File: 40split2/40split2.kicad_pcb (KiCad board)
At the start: 2 copper layers, 145.3 x 97 mm, 54 parts

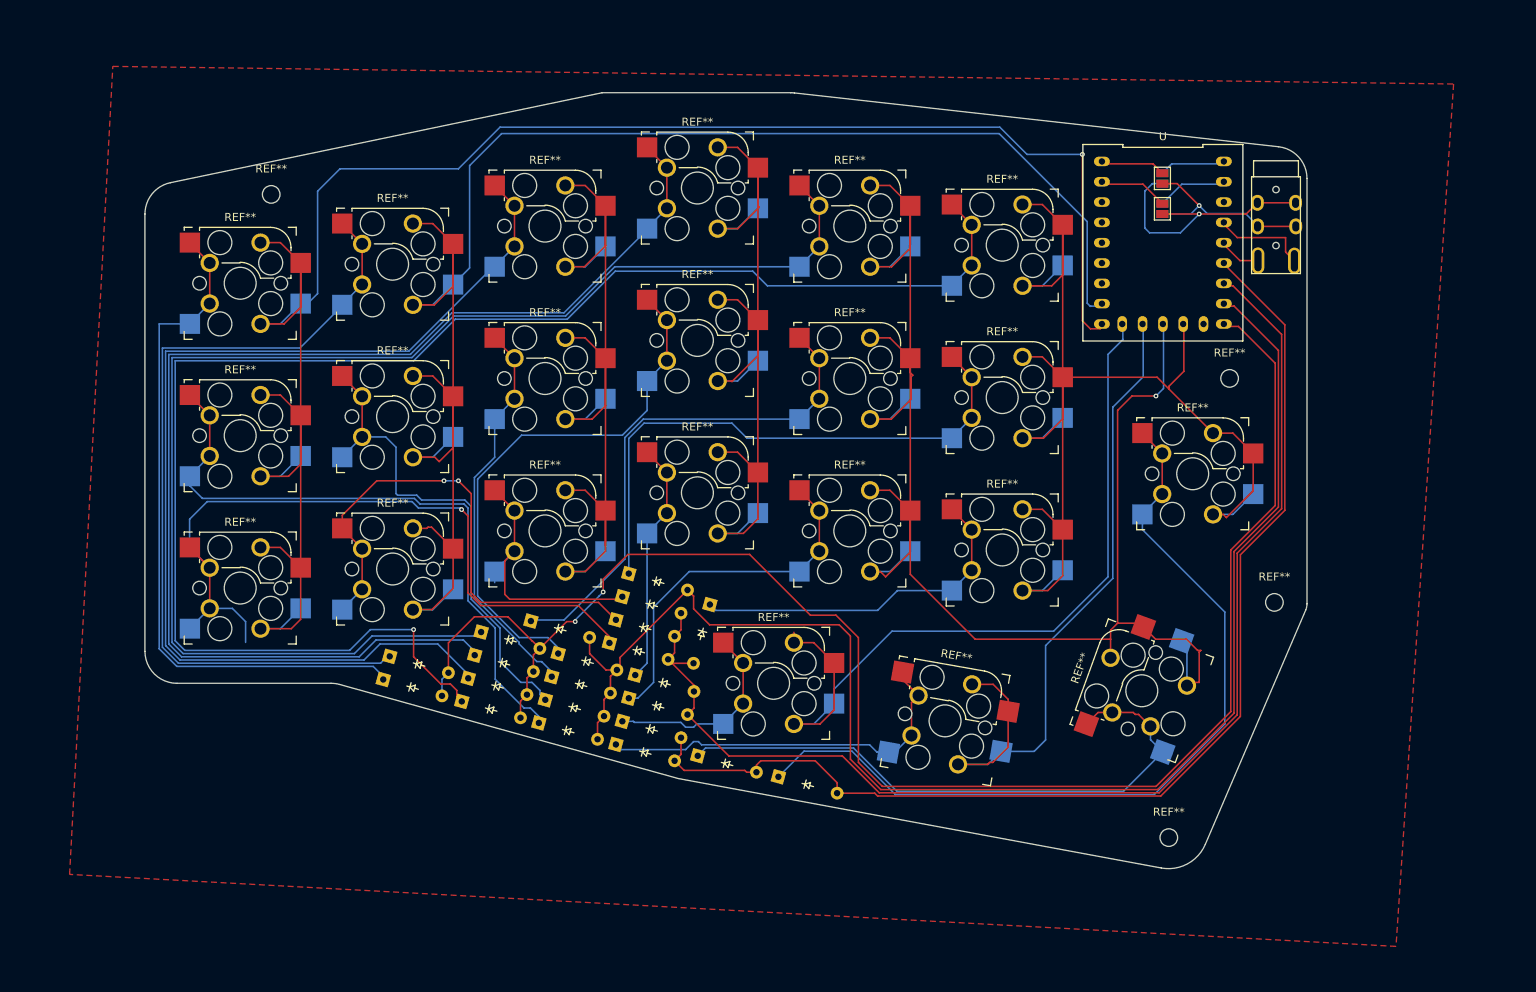
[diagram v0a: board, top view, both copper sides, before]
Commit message: Keyboard V4: Rearrange diodes
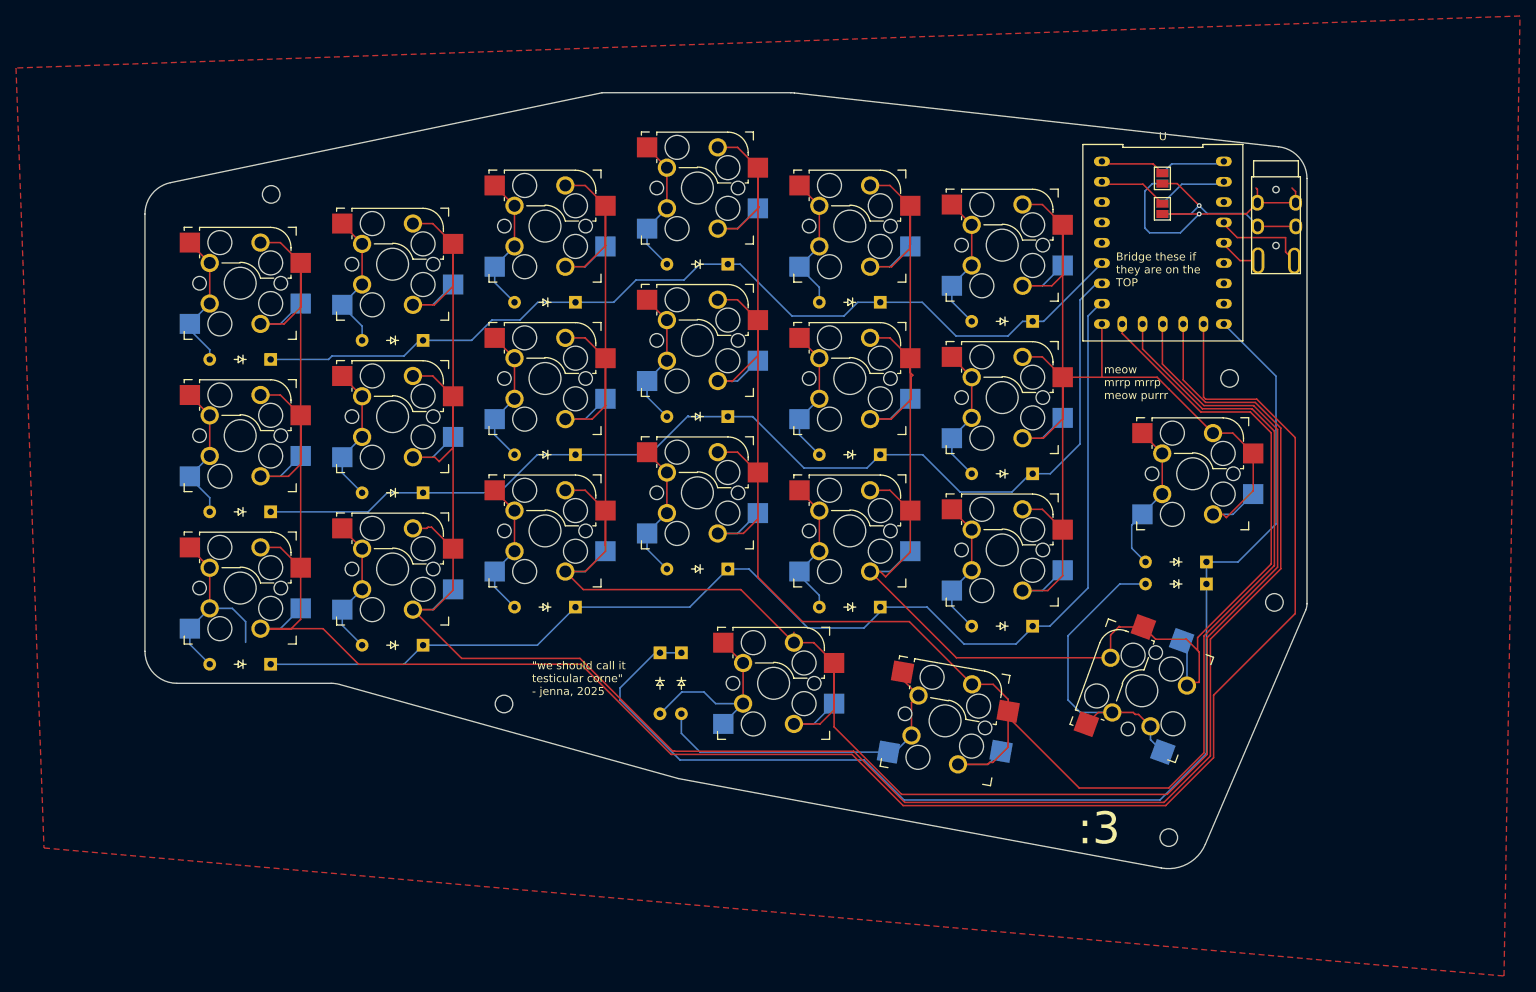
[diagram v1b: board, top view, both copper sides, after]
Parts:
- removed the REF** at (121.8, 134.7)
- removed the REF** at (114.6, 123.4)
- removed the REF** at (131.5, 137.4)
- removed the REF** at (143.2, 119.9)
- removed the REF** at (151.8, 141.5)
- removed the REF** at (112.2, 132.0)
- removed the REF** at (123.5, 129.0)
- removed the REF** at (122.7, 131.8)
- removed the REF** at (120.9, 122.0)
- removed the REF** at (133.1, 131.6)
- removed the REF** at (113.0, 129.2)
- removed the REF** at (124.3, 126.1)
- removed the REF** at (113.8, 126.3)
- removed the REF** at (133.9, 128.8)
- removed the REF** at (133.1, 116.1)
- removed the REF** at (141.7, 138.8)
- removed the REF** at (103.2, 126.4)
- removed the REF** at (131.5, 121.8)
- removed the REF** at (102.4, 129.3)
- removed the REF** at (130.7, 124.7)
- removed the REF** at (132.3, 119.0)
- removed the REF** at (132.3, 134.5)
- added REF**: 1N4148, Scotto_lib:Diode_DO-35, F.Cu at (164.5, 101.2)
- added REF**: 1N4148, Scotto_lib:Diode_DO-35, F.Cu at (126.4, 120.3)
- added REF**: 1N4148, Scotto_lib:Diode_DO-35, F.Cu at (139.7, 126.0)
- added REF**: 1N4148, Scotto_lib:Diode_DO-35, F.Cu at (164.5, 120.3)
- added REF**: 1N4148, Scotto_lib:Diode_DO-35, F.Cu at (145.5, 96.4)
- added REF**: MountingHole_2.2mm_M2, kicad_screws:MountingHole_2.2mm_M2, F.Cu at (117.5, 132.4)
- added REF**: 1N4148, Scotto_lib:Diode_DO-35, F.Cu at (107.4, 106.0)
- added REF**: 1N4148, Scotto_lib:Diode_DO-35, F.Cu at (183.6, 103.6)
- added REF**: 1N4148, Scotto_lib:Diode_DO-35, F.Cu at (107.4, 86.9)
- added REF**: 1N4148, Scotto_lib:Diode_DO-35, F.Cu at (107.4, 125.0)
- added REF**: 1N4148, Scotto_lib:Diode_DO-35, F.Cu at (164.5, 82.2)
- added REF**: 1N4148, Scotto_lib:Diode_DO-35, F.Cu at (183.6, 84.5)
- added REF**: 1N4148, Scotto_lib:Diode_DO-35, F.Cu at (205.3, 114.6)
- added REF**: 1N4148, Scotto_lib:Diode_DO-35, F.Cu at (126.4, 101.2)
- added REF**: 1N4148, Scotto_lib:Diode_DO-35, F.Cu at (205.3, 117.4)
- added REF**: 1N4148, Scotto_lib:Diode_DO-35, F.Cu at (126.4, 82.2)
- added REF**: 1N4148, Scotto_lib:Diode_DO-35, F.Cu at (88.3, 108.4)
- added REF**: 1N4148, Scotto_lib:Diode_DO-35, F.Cu at (88.3, 89.3)
- added REF**: 1N4148, Scotto_lib:Diode_DO-35, F.Cu at (88.3, 127.4)
- added REF**: 1N4148, Scotto_lib:Diode_DO-35, F.Cu at (145.5, 77.4)
- added REF**: 1N4148, Scotto_lib:Diode_DO-35, F.Cu at (145.5, 115.5)
- added REF**: 1N4148, Scotto_lib:Diode_DO-35, F.Cu at (137.0, 126.0)
- added REF**: 1N4148, Scotto_lib:Diode_DO-35, F.Cu at (183.6, 122.6)
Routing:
- net (no net): track 3853.1 -> 2673.8 mm, vias 10 -> 2
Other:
- board text added: ":3"
- board text added: ":3 :3 :3"
- board text added: "Bridge these if they are on the TOP"
- board text added: "github.com/junnnaaaaaa github.com/HamNuggets"
- board text added: "meow mrrp mrrp meow purrr"
- board text added: "{dblquote}We are NOT calling it testicular corne{dblquote} - jade, 2025"
- board text added: "{dblquote}we should call it testicular corne{dblquote} - jenna, 2025"

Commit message: qmk begins.. a battle awaits
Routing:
- net (no net): track 2673.8 -> 2673.2 mm
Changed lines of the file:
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@@
-	)
-	(segment
-		(start 209.14625 74.07)
-		(end 207.55 72.47375)
-		(width 0.2)
-		(layer "F.Cu")
-		(net 0)
 	)
 	(segment
@@
 	)
 	(segment
+		(start 211.665 67.695)
+		(end 211.99 67.37)
+		(width 0.2)
+		(layer "F.Cu")
+		(net 0)
+	)
+	(segment
 		(start 92.075 96.28625)
 		(end 92.075 102.385)
@@
 	)
 	(segment
+		(start 213.15 74.71)
+		(end 213.49 74.37)
+		(width 0.2)
+		(layer "F.Cu")
+		(net 0)
+	)
+	(segment
 		(start 106.105 120.575)
 		(end 112.2 126.67)
@@
 	)
 	(segment
-		(start 215.19 75.87)
-		(end 215.19 74.07)
-		(width 0.2)
-		(layer "F.Cu")
-		(net 0)
-	)
-	(segment
 		(start 158.75 127.2425)
 		(end 158.75 135.23)
@@
 	)
 	(segment
-		(start 216.44 68.32)
-		(end 215.99 67.87)
-		(width 0.2)
-		(layer "F.Cu")
-		(net 0)
-	)
-	(segment
 		(start 154.425 86.6025)
 		(end 154.425 86.6625)
@@
 	)
 	(segment
+		(start 214.49 74.37)
+		(end 216.29 76.17)
+		(width 0.2)
+		(layer "F.Cu")
+		(net 0)
+	)
+	(segment
 		(start 175.955 72.47375)
 		(end 175.955 77.55375)
@@
 	)
 	(segment
+		(start 216.44 67.82)
+		(end 215.99 67.37)
+		(width 0.2)
+		(layer "F.Cu")
+		(net 0)
+	)
+	(segment
 		(start 87.055 84.85625)
 		(end 90.00375 84.85625)
@@
 	)
 	(segment
-		(start 211.665 68.045)
-		(end 211.49 67.87)
-		(width 0.2)
-		(layer "F.Cu")
-		(net 0)
-	)
-	(segment
 		(start 168.19 75.07)
 		(end 168.275 74.985)
@@
 	)
 	(segment
-		(start 216.44 69.72)
-		(end 216.44 68.32)
-		(width 0.2)
-		(layer "F.Cu")
-		(net 0)
-	)
-	(segment
 		(start 192.31 67.39375)
 		(end 197.36375 67.39375)
@@
 	)
 	(segment
+		(start 216.29 76.17)
+		(end 216.29 76.97)
+		(width 0.2)
+		(layer "F.Cu")
+		(net 0)
+	)
+	(segment
 		(start 192.19 91.52375)
 		(end 199.1325 91.52375)
@@
 	)
 	(segment
-		(start 215.19 74.07)
-		(end 209.14625 74.07)
-		(width 0.2)
-		(layer "F.Cu")
-		(net 0)
-	)
-	(segment
 		(start 173.475 69.93375)
 		(end 173.475 69.99375)
@@
 	)
 	(segment
-		(start 211.665 69.72)
-		(end 211.665 68.045)
-		(width 0.2)
-		(layer "F.Cu")
-		(net 0)
-	)
-	(segment
 		(start 180.507463 133.987463)
 		(end 180.507463 133.285665)
@@
 	)
 	(segment
+		(start 207.47 77.25)
+		(end 211.435 77.25)
+		(width 0.2)
+		(layer "F.Cu")
+		(net 0)
+	)
+	(segment
 		(start 190.291445 134.888403)
 		(end 191.753151 133.426697)
@@
 	)
 	(segment
+		(start 213.49 74.37)
+		(end 214.49 74.37)
+		(width 0.2)
+		(layer "F.Cu")
+		(net 0)
+	)
+	(segment
 		(start 153.73 124.7025)
 		(end 156.21 124.7025)
@@
 	)
 	(segment
+		(start 216.44 69.72)
+		(end 216.44 67.82)
+		(width 0.2)
+		(layer "F.Cu")
+		(net 0)
+	)
+	(segment
 		(start 167.59 144.67)
 		(end 199.99 144.67)
@@
 	)
 	(segment
-		(start 211.74 76.945)
-		(end 209.48125 76.945)
-		(width 0.2)
-		(layer "F.Cu")
-		(net 0)
-	)
-	(segment
 		(start 130.175 89.1425)
 		(end 130.175 95.085)
@@
 	)
 	(segment
-		(start 216.29 76.97)
-		(end 215.19 75.87)
-		(width 0.2)
-		(layer "F.Cu")
-		(net 0)
-	)
-	(segment
 		(start 156.21 124.7025)
 		(end 158.75 127.2425)
@@
 	)
 	(segment
+		(start 211.435 77.25)
+		(end 211.74 76.945)
+		(width 0.2)
+		(layer "F.Cu")
+		(net 0)
+	)
+	(segment
 		(start 78.225 112.79625)
 		(end 78.225 112.85625)
@@
 	)
 	(segment
+		(start 207.47 74.71)
+		(end 213.15 74.71)
+		(width 0.2)
+		(layer "F.Cu")
+		(net 0)
+	)
+	(segment
 		(start 175.955 110.57375)
 		(end 175.955 115.65375)
@@
 	)
 	(segment
-		(start 209.48125 76.945)
-		(end 207.55 75.01375)
-		(width 0.2)
-		(layer "F.Cu")
-		(net 0)
-	)
-	(segment
 		(start 204.99 95.07)
 		(end 199.79 89.87)
@@
 		(width 0.2)
 		(layer "F.Cu")
+		(net 0)
+	)
+	(segment
+		(start 211.665 69.72)
+		(end 211.665 67.695)
+		(width 0.2)
+		(layer "F.Cu")
